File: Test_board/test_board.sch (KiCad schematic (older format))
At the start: 36 parts, among them J1 CONN_02X26, J17 Conn_01x02, J18 TEST_1P, J2 CONN_02X26, J3 Conn_02x05_Odd_Even, J4 Conn_01x03, J5 Conn_02x20_Odd_Even, J6 DB9_Male, J7 Conn_01x06, J8 Conn_02x20_Odd_Even, J9 USB_A, Q1 Q_NMOS_GSD, U1 STM32F303RE, U12 MS5540C, U2 24LC256, U6 MAX6730A

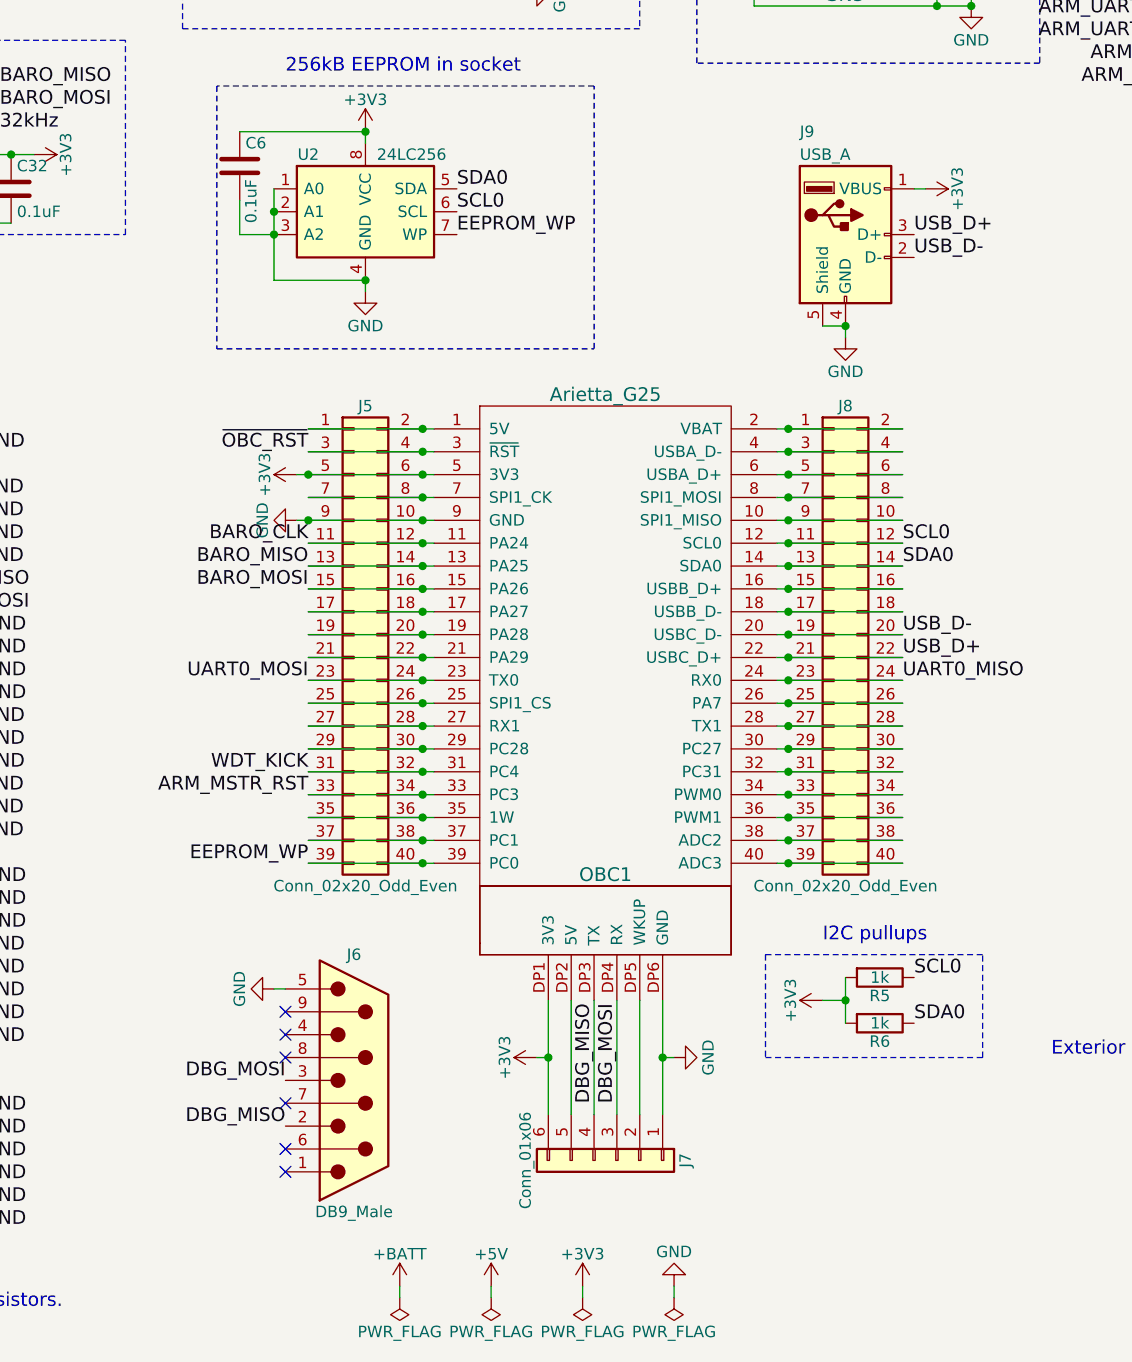
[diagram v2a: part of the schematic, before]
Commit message: Removed db9, created last footprints, finished assigning footprints, started pcb
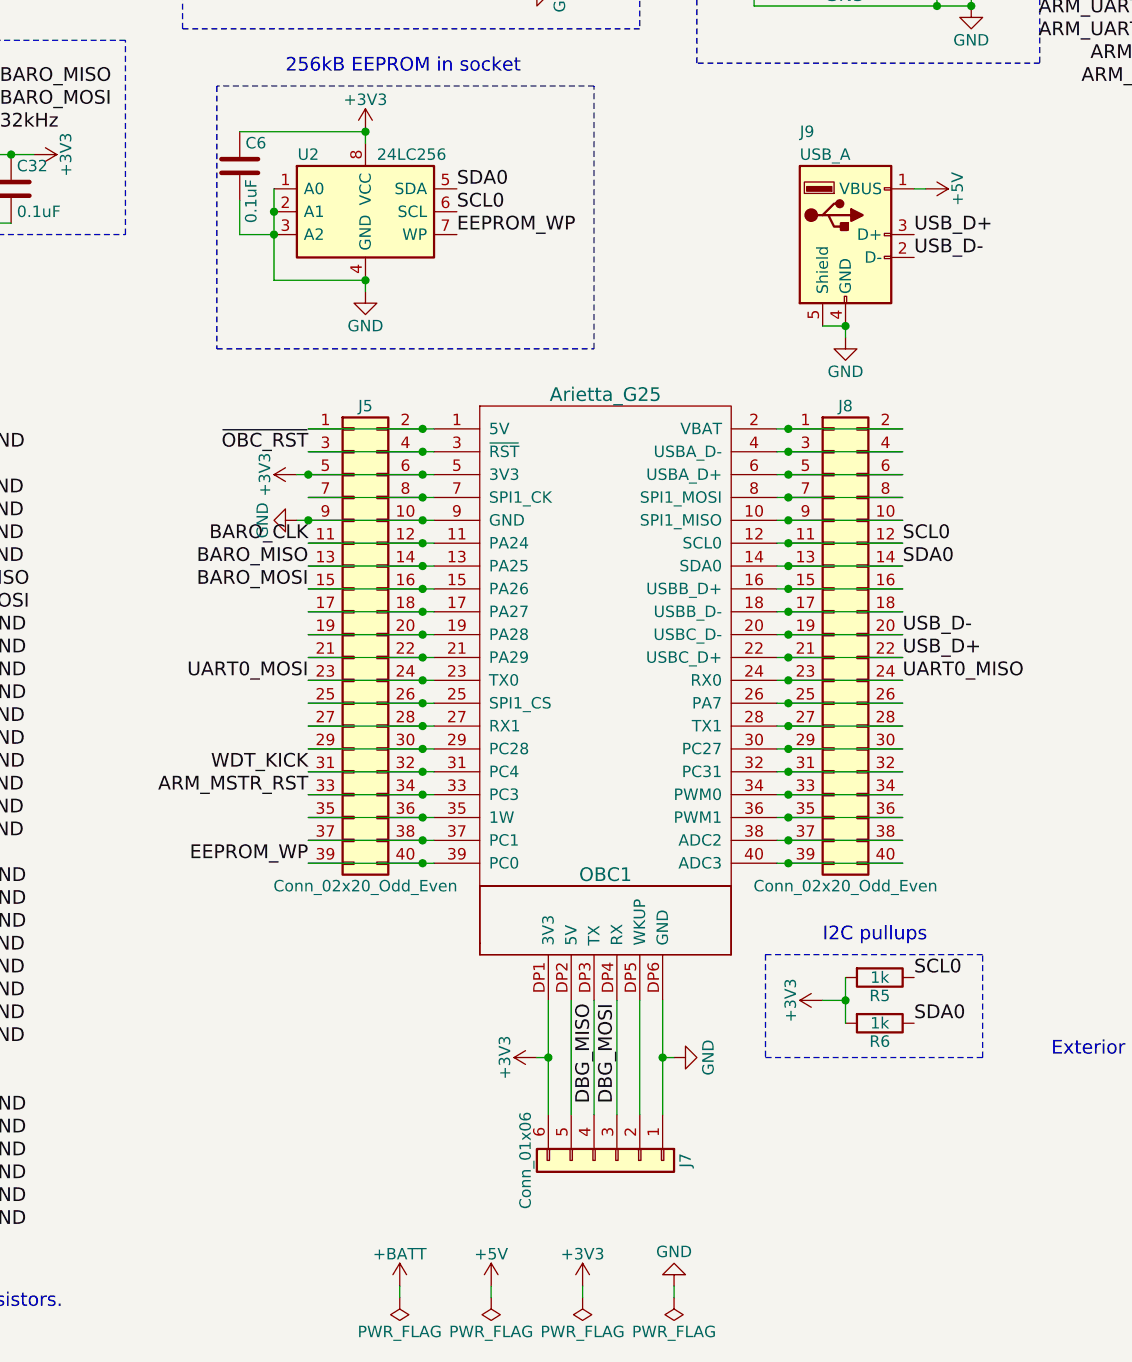
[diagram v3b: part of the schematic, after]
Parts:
- removed J6: DB9_Male, symbol DB9_Male
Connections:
- net +3V3: no longer J9.1 (VBUS)
- net +5V: now also J9.1 (VBUS)
- no-connect marks 50 -> 44
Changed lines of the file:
@@
 Sheet 1 2
 Title "ARIETTA TEST BOARD"
-Date ""
+Date "2017-11-08"
 Rev "2"
 Comp ""
 Comment1 "D. FERNIE"
-Comment2 ""
+Comment2 "D. FERNIE"
 Comment3 ""
 Comment4 ""
@@
 $EndComp
 $Comp
-L +3V3 #PWR010
-U 1 1 59FA69EC
-P 8400 2800
-F 0 "#PWR010" H 8400 2650 50  0001 C CNN
-F 1 "+3V3" H 8400 2940 50  0000 C CNN
-F 2 "" H 8400 2800 50  0001 C CNN
-F 3 "" H 8400 2800 50  0001 C CNN
-	1    8400 2800
-	0    1    1    0
-$EndComp
-$Comp
-L DB9_Male J6
-U 1 1 59FA6CEA
-P 5900 6700
-F 0 "J6" H 5900 7250 50  0000 C CNN
-F 1 "DB9_Male" H 5900 6125 50  0000 C CNN
-F 2 "" H 5900 6700 50  0001 C CNN
-F 3 "" H 5900 6700 50  0001 C CNN
-	1    5900 6700
-	1    0    0    -1
-$EndComp
-Text Label 5600 6700 2    60   ~ 0
-DBG_MOSI
-Text Label 5600 6900 2    60   ~ 0
-DBG_MISO
-$Comp
 L GND #PWR011
-U 1 1 59FA6FDF
-P 5550 6300
-F 0 "#PWR011" H 5550 6050 50  0001 C CNN
-F 1 "GND" H 5550 6150 50  0000 C CNN
-F 2 "" H 5550 6300 50  0001 C CNN
-F 3 "" H 5550 6300 50  0001 C CNN
-	1    5550 6300
-	0    1    1    0
-$EndComp
-NoConn ~ 5600 6400
-NoConn ~ 5600 6500
-NoConn ~ 5600 6800
-NoConn ~ 5600 7000
-NoConn ~ 5600 7100
-$Comp
-L GND #PWR012
 U 1 1 59FA7E5E
 P 9600 3900
-F 0 "#PWR012" H 9600 3650 50  0001 C CNN
+F 0 "#PWR011" H 9600 3650 50  0001 C CNN
 F 1 "GND" H 9600 3750 50  0000 C CNN
 F 2 "" H 9600 3900 50  0001 C CNN
@@
 $EndComp
 $Comp
-L +3V3 #PWR013
+L +3V3 #PWR012
 U 1 1 59FA7FAE
 P 9600 950
-F 0 "#PWR013" H 9600 800 50  0001 C CNN
+F 0 "#PWR012" H 9600 800 50  0001 C CNN
 F 1 "+3V3" H 9600 1090 50  0000 C CNN
 F 2 "" H 9600 950 50  0001 C CNN
@@
 ARM_SWDIO
 $Comp
-L +3V3 #PWR014
+L +3V3 #PWR013
 U 1 1 59FA9570
 P 1700 6100
-F 0 "#PWR014" H 1700 5950 50  0001 C CNN
+F 0 "#PWR013" H 1700 5950 50  0001 C CNN
 F 1 "+3V3" H 1700 6240 50  0000 C CNN
 F 2 "" H 1700 6100 50  0001 C CNN
@@
 $EndComp
 $Comp
-L GND #PWR015
+L GND #PWR014
 U 1 1 59FA95A2
 P 600 6000
-F 0 "#PWR015" H 600 5750 50  0001 C CNN
+F 0 "#PWR014" H 600 5750 50  0001 C CNN
 F 1 "GND" H 600 5850 50  0000 C CNN
 F 2 "" H 600 6000 50  0001 C CNN
@@
 $EndComp
 $Comp
-L +5V #PWR016
+L +5V #PWR015
 U 1 1 59FA999D
 P 700 6200
-F 0 "#PWR016" H 700 6050 50  0001 C CNN
+F 0 "#PWR015" H 700 6050 50  0001 C CNN
 F 1 "+5V" H 700 6340 50  0000 C CNN
 F 2 "" H 700 6200 50  0001 C CNN
@@
 $EndComp
 $Comp
-L PWR_FLAG #FLG017
+L PWR_FLAG #FLG016
 U 1 1 59FA9A77
 P 6500 7650
-F 0 "#FLG017" H 6500 7725 50  0001 C CNN
+F 0 "#FLG016" H 6500 7725 50  0001 C CNN
 F 1 "PWR_FLAG" H 6500 7800 50  0000 C CNN
 F 2 "" H 6500 7650 50  0001 C CNN
@@
 $EndComp
 $Comp
-L +5V #PWR018
+L +5V #PWR017
 U 1 1 59FA9AA7
 P 6500 7600
-F 0 "#PWR018" H 6500 7450 50  0001 C CNN
+F 0 "#PWR017" H 6500 7450 50  0001 C CNN
 F 1 "+5V" H 6500 7740 50  0000 C CNN
 F 2 "" H 6500 7600 50  0001 C CNN
@@
 $EndComp
 $Comp
-L GND #PWR019
+L GND #PWR018
 U 1 1 59FAB991
 P 2600 3600
-F 0 "#PWR019" H 2600 3350 50  0001 C CNN
+F 0 "#PWR018" H 2600 3350 50  0001 C CNN
 F 1 "GND" H 2600 3450 50  0000 C CNN
 F 2 "" H 2600 3600 50  0001 C CNN
@@
 $EndComp
 $Comp
-L +3V3 #PWR020
+L +3V3 #PWR019
 U 1 1 59FABA66
 P 2400 3600
-F 0 "#PWR020" H 2400 3450 50  0001 C CNN
+F 0 "#PWR019" H 2400 3450 50  0001 C CNN
 F 1 "+3V3" H 2400 3740 50  0000 C CNN
 F 2 "" H 2400 3600 50  0001 C CNN
@@
 Text Label 3950 4650 0    60   ~ 0
 UART0_MOSI
-NoConn ~ 5600 6600
 Text Label 2500 7150 2    60   ~ 0
 ARM_SWDIO
@@
 T_MCU_GND
 $Comp
-L GND #PWR021
+L GND #PWR020
 U 1 1 59FBB9F5
 P 1000 7400
-F 0 "#PWR021" H 1000 7150 50  0001 C CNN
+F 0 "#PWR020" H 1000 7150 50  0001 C CNN
 F 1 "GND" H 1000 7250 50  0000 C CNN
 F 2 "" H 1000 7400 50  0001 C CNN
@@
 	8400 2800 8350 2800
 Wire Wire Line
-	5550 6300 5600 6300
-Wire Wire Line
 	9600 950  10150 950
 Wire Wire Line
@@
 	8450 1500 8450 1600
 $Comp
-L GND #PWR022
+L GND #PWR021
 U 1 1 59FBFBE8
 P 8600 2000
-F 0 "#PWR022" H 8600 1750 50  0001 C CNN
+F 0 "#PWR021" H 8600 1750 50  0001 C CNN
 F 1 "GND" H 8600 1850 50  0000 C CNN
 F 2 "" H 8600 2000 50  0001 C CNN
@@
 $EndComp
 $Comp
-L GND #PWR023
+L GND #PWR022
 U 1 1 59FBFC2A
 P 8600 1250
-F 0 "#PWR023" H 8600 1000 50  0001 C CNN
+F 0 "#PWR022" H 8600 1000 50  0001 C CNN
 F 1 "GND" H 8600 1100 50  0000 C CNN
 F 2 "" H 8600 1250 50  0001 C CNN
@@
 Connection ~ 8450 2000
 $Comp
-L +3V3 #PWR024
+L +3V3 #PWR023
 U 1 1 59FBFEB7
 P 8700 1550
-F 0 "#PWR024" H 8700 1400 50  0001 C CNN
+F 0 "#PWR023" H 8700 1400 50  0001 C CNN
 F 1 "+3V3" H 8700 1690 50  0000 C CNN
 F 2 "" H 8700 1550 50  0001 C CNN
@@
 $EndComp
 $Comp
-L +3V3 #PWR025
+L +3V3 #PWR024
 U 1 1 59FBFEF9
 P 8700 750
-F 0 "#PWR025" H 8700 600 50  0001 C CNN
+F 0 "#PWR024" H 8700 600 50  0001 C CNN
 F 1 "+3V3" H 8700 890 50  0000 C CNN
 F 2 "" H 8700 750 50  0001 C CNN
@@
 Connection ~ 5600 1400
 $Comp
-L GND #PWR026
+L GND #PWR025
 U 1 1 59FC5704
 P 5550 850
-F 0 "#PWR026" H 5550 600 50  0001 C CNN
+F 0 "#PWR025" H 5550 600 50  0001 C CNN
 F 1 "GND" H 5550 700 50  0000 C CNN
 F 2 "" H 5550 850 50  0001 C CNN
@@
 $EndComp
 $Comp
-L GND #PWR027
+L GND #PWR026
 U 1 1 59FC5746
 P 6850 900
-F 0 "#PWR027" H 6850 650 50  0001 C CNN
+F 0 "#PWR026" H 6850 650 50  0001 C CNN
 F 1 "GND" H 6850 750 50  0000 C CNN
 F 2 "" H 6850 900 50  0001 C CNN
@@
 EEPROM_WP
 $Comp
-L GND #PWR028
+L GND #PWR027
 U 1 1 59FCB62A
 P 5950 3250
-F 0 "#PWR028" H 5950 3000 50  0001 C CNN
+F 0 "#PWR027" H 5950 3000 50  0001 C CNN
 F 1 "GND" H 5950 3100 50  0000 C CNN
 F 2 "" H 5950 3250 50  0001 C CNN
@@
 Connection ~ 5950 3200
 $Comp
-L +3V3 #PWR029
+L +3V3 #PWR028
 U 1 1 59FCBA77
 P 5950 2550
-F 0 "#PWR029" H 5950 2400 50  0001 C CNN
+F 0 "#PWR028" H 5950 2400 50  0001 C CNN
 F 1 "+3V3" H 5950 2690 50  0000 C CNN
 F 2 "" H 5950 2550 50  0001 C CNN
@@
 Connection ~ 10150 6300
 $Comp
-L +BATT #PWR030
+L +BATT #PWR029
 U 1 1 59FD1075
 P 10150 3500
-F 0 "#PWR030" H 10150 3350 50  0001 C CNN
+F 0 "#PWR029" H 10150 3350 50  0001 C CNN
 F 1 "+BATT" H 10150 3640 50  0000 C CNN
 F 2 "" H 10150 3500 50  0001 C CNN
@@
 Connection ~ 10150 3450
 $Comp
-L GND #PWR031
+L GND #PWR030
 U 1 1 59FD1678
 P 10200 6400
-F 0 "#PWR031" H 10200 6150 50  0001 C CNN
+F 0 "#PWR030" H 10200 6150 50  0001 C CNN
 F 1 "GND" H 10200 6250 50  0000 C CNN
 F 2 "" H 10200 6400 50  0001 C CNN
@@
 Connection ~ 10150 6400
 $Comp
-L PWR_FLAG #FLG032
+L PWR_FLAG #FLG031
 U 1 1 59FD1C7D
 P 6100 7650
-F 0 "#FLG032" H 6100 7725 50  0001 C CNN
+F 0 "#FLG031" H 6100 7725 50  0001 C CNN
 F 1 "PWR_FLAG" H 6100 7800 50  0000 C CNN
 F 2 "" H 6100 7650 50  0001 C CNN
@@
 $EndComp
 $Comp
-L +BATT #PWR033
+L +BATT #PWR032
 U 1 1 59FD1CC7
 P 6100 7600
-F 0 "#PWR033" H 6100 7450 50  0001 C CNN
+F 0 "#PWR032" H 6100 7450 50  0001 C CNN
 F 1 "+BATT" H 6100 7740 50  0000 C CNN
 F 2 "" H 6100 7600 50  0001 C CNN
@@
 ~OBC_RST
 $Comp
-L +3V3 #PWR034
+L +3V3 #PWR033
 U 1 1 59FCD5B1
 P 4750 1100
-F 0 "#PWR034" H 4750 950 50  0001 C CNN
+F 0 "#PWR033" H 4750 950 50  0001 C CNN
 F 1 "+3V3" H 4750 1240 50  0000 C CNN
 F 2 "" H 4750 1100 50  0001 C CNN
@@
 	4150 1100 4650 1100
 $Comp
-L GND #PWR035
+L GND #PWR034
 U 1 1 59FCD717
 P 3300 1200
-F 0 "#PWR035" H 3300 950 50  0001 C CNN
+F 0 "#PWR034" H 3300 950 50  0001 C CNN
 F 1 "GND" H 3300 1050 50  0000 C CNN
 F 2 "" H 3300 1200 50  0001 C CNN
@@
 SDA0
 $Comp
-L +3V3 #PWR036
+L +3V3 #PWR035
 U 1 1 59FCFCD9
 P 7950 6350
-F 0 "#PWR036" H 7950 6200 50  0001 C CNN
+F 0 "#PWR035" H 7950 6200 50  0001 C CNN
 F 1 "+3V3" H 7950 6490 50  0000 C CNN
 F 2 "" H 7950 6350 50  0001 C CNN
@@
 Connection ~ 4250 1100
 $Comp
-L GND #PWR037
+L GND #PWR036
 U 1 1 59FF625D
 P 4600 950
-F 0 "#PWR037" H 4600 700 50  0001 C CNN
+F 0 "#PWR036" H 4600 700 50  0001 C CNN
 F 1 "GND" H 4600 800 50  0000 C CNN
 F 2 "" H 4600 950 50  0001 C CNN
@@
 $EndComp
 $Comp
-L +3V3 #PWR038
+L +3V3 #PWR037
 U 1 1 5A00FDFA
 P 4500 2650
-F 0 "#PWR038" H 4500 2500 50  0001 C CNN
+F 0 "#PWR037" H 4500 2500 50  0001 C CNN
 F 1 "+3V3" H 4500 2790 50  0000 C CNN
 F 2 "" H 4500 2650 50  0001 C CNN
@@
 Connection ~ 4400 2650
 $Comp
-L GND #PWR039
+L GND #PWR038
 U 1 1 5A01044D
 P 3400 2450
-F 0 "#PWR039" H 3400 2200 50  0001 C CNN
+F 0 "#PWR038" H 3400 2200 50  0001 C CNN
 F 1 "GND" H 3400 2300 50  0000 C CNN
 F 2 "" H 3400 2450 50  0001 C CNN
@@
 	10150 2750 9650 2750
 $Comp
-L GND #PWR040
+L GND #PWR039
 U 1 1 5A01F2D3
 P 10200 2150
-F 0 "#PWR040" H 10200 1900 50  0001 C CNN
+F 0 "#PWR039" H 10200 1900 50  0001 C CNN
 F 1 "GND" H 10200 2000 50  0000 C CNN
 F 2 "" H 10200 2150 50  0001 C CNN
@@
 	5300 1000 5600 1000
 $Comp
-L GND #PWR041
+L GND #PWR040
 U 1 1 5A0254FB
 P 6650 1950
-F 0 "#PWR041" H 6650 1700 50  0001 C CNN
+F 0 "#PWR040" H 6650 1700 50  0001 C CNN
 F 1 "GND" H 6650 1800 50  0000 C CNN
 F 2 "" H 6650 1950 50  0001 C CNN
@@
 Connection ~ 6600 1950
 $Comp
-L +3V3 #PWR042
+L +3V3 #PWR041
 U 1 1 5A0274EB
 P 5250 1100
-F 0 "#PWR042" H 5250 950 50  0001 C CNN
+F 0 "#PWR041" H 5250 950 50  0001 C CNN
 F 1 "+3V3" H 5250 1240 50  0000 C CNN
 F 2 "" H 5250 1100 50  0001 C CNN
@@
 NoConn ~ 900  5850
 $Comp
-L GND #PWR043
+L GND #PWR042
 U 1 1 5A02A303
 P 2100 5050
-F 0 "#PWR043" H 2100 4800 50  0001 C CNN
+F 0 "#PWR042" H 2100 4800 50  0001 C CNN
 F 1 "GND" H 2100 4900 50  0000 C CNN
 F 2 "" H 2100 5050 50  0001 C CNN
@@
 	2100 5050 2100 5000
 $Comp
-L +3V3 #PWR044
+L +3V3 #PWR043
 U 1 1 5A02A559
 P 2100 4650
-F 0 "#PWR044" H 2100 4500 50  0001 C CNN
+F 0 "#PWR043" H 2100 4500 50  0001 C CNN
 F 1 "+3V3" H 2100 4790 50  0000 C CNN
 F 2 "" H 2100 4650 50  0001 C CNN
@@
 Wire Wire Line
 	2100 4650 2100 4700
+$Comp
+L +5V #PWR?
+U 1 1 5A03D1A9
+P 8400 2800
+F 0 "#PWR?" H 8400 2650 50  0001 C CNN
+F 1 "+5V" H 8400 2940 50  0000 C CNN
+F 2 "" H 8400 2800 50  0001 C CNN
+F 3 "" H 8400 2800 50  0001 C CNN
+	1    8400 2800
+	0    1    1    0
+$EndComp
 $EndSCHEMATC

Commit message: finished pcb
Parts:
- removed J9: USB_A, aleksandr_footprints:USB_A_Board, symbol USB_A
- added C33: 0.1uF, Capacitors_SMD:C_0805_HandSoldering, symbol C
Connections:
- net +3V3: now also C33.1
- net ARM_SPI1_MISO: no longer U1.22 (PA6)
- net ARM_SPI1_MOSI: no longer U1.23 (PA7)
- net ARM_SPI1_SCK: no longer U1.21 (PA5)
- net ARM_UART2_MISO: no longer U1.16 (PA2)
- net ARM_UART2_MOSI: no longer U1.17 (PA3)
- net ARM_USB_D+: no longer U1.45 (PA12)
- net ARM_USB_D-: no longer U1.44 (PA11)
- net B_MCU_GND: now also U1.21 (PA5), U1.22 (PA6), U1.23 (PA7), U1.44 (PA11), U1.45 (PA12)
- net CAN_RX: no longer U1.61 (PB8)
- net CAN_TX: no longer U1.62 (PB9)
- net GND: now also C33.2
- net L_MCU_GND: now also U1.16 (PA2), U1.17 (PA3)
- net T_MCU_GND: now also U1.61 (PB8), U1.62 (PB9)
- net USB_D+: no longer names the net of J8.21 (Pin_21), J8.22 (Pin_22), OBC1.22 (USBC_D+)
- net USB_D-: no longer names the net of J8.19 (Pin_19), J8.20 (Pin_20), OBC1.20 (USBC_D-)
